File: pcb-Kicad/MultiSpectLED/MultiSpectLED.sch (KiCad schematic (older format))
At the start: 117 parts, among them J1 Conn_01x02_Female, J2 USB_C_Receptacle_USB2.0, SW1 NKK_HEXADEC, SW2 NKK_HEXADEC, U1 PAM2804, U10 PAM2804, U11 PAM2804, U12 PAM2804, U13 PAM2804, U14 PAM2804, U15 PAM2804, U16 PAM2804, U2 TeensyLC, U3 PAM2804, U4 PAM2804, U5 PAM2804, U6 PAM2804, U7 PAM2804, U8 PAM2804, U9 PAM2804

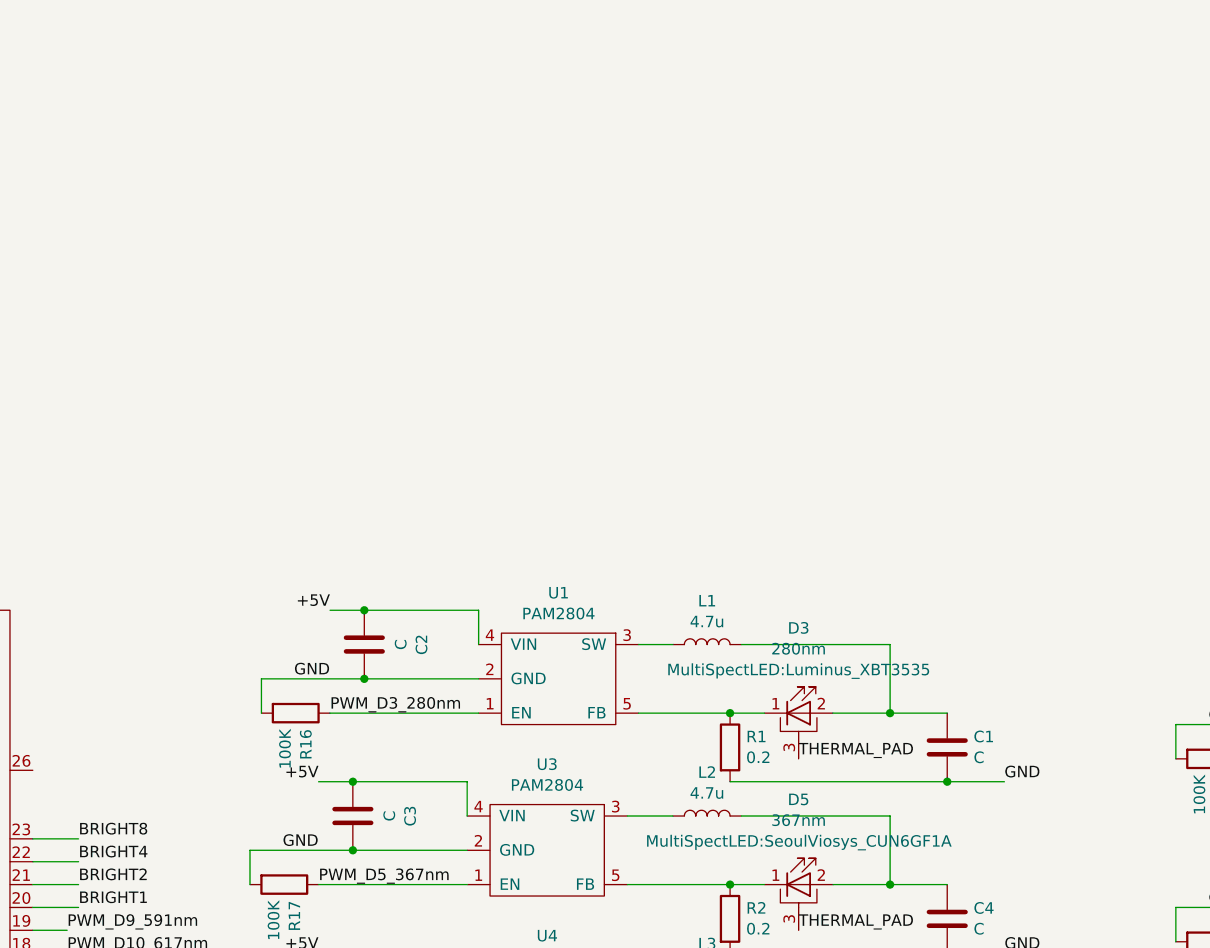
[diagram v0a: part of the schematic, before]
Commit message: Use boost driver for 280nm LED
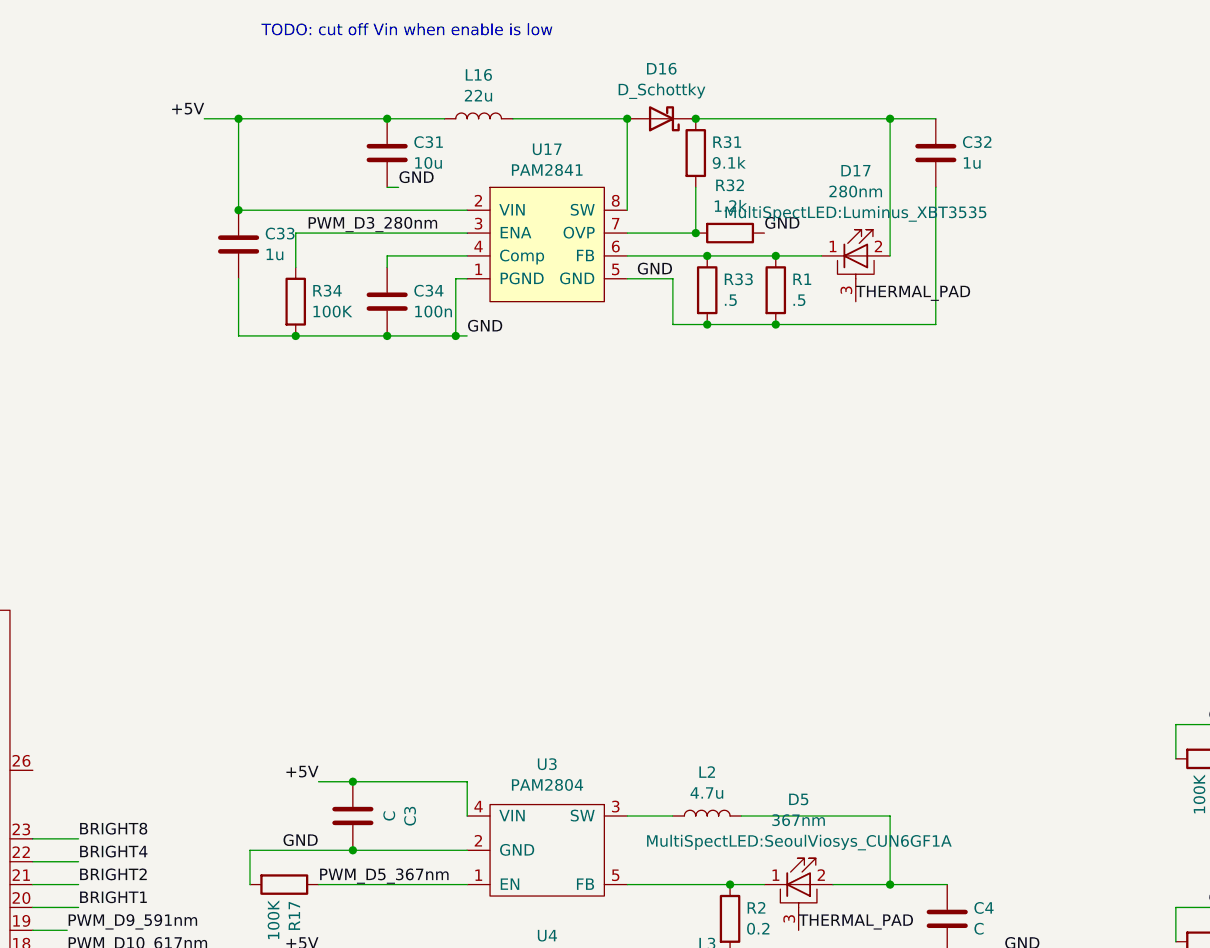
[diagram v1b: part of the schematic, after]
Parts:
- removed C1, C2: C, MultiSpectLED:C_0805_2012Metric, symbol MultiSpectLED:C
- removed D3: 280nm, MultiSpectLED:Luminus_XBT3535, symbol MultiSpectLED:LED_PAD
- removed L1: 4.7u, MultiSpectLED:L_1007_2518Metric, symbol MultiSpectLED:L
- removed R1: 0.2, MultiSpectLED:R_0805_2012Metric, symbol MultiSpectLED:R
- removed R16: 100K, MultiSpectLED:R_0402_1005Metric, symbol MultiSpectLED:R
- removed U1: PAM2804, MultiSpectLED:SOT-23-5, symbol MultiSpectLED:PAM2804
- added C31: 10u, MultiSpectLED:C_0805_2012Metric, symbol Device:C
- added C32, C33: 1u, MultiSpectLED:C_0805_2012Metric, symbol Device:C
- added C34: 100n, Capacitor_SMD:C_0402_1005Metric, symbol Device:C
- added D16: D_Schottky, Diode_SMD:D_TUMD2, symbol Device:D_Schottky
- added D17: 280nm, MultiSpectLED:Luminus_XBT3535, symbol MultiSpectLED:LED_PAD
- added L16: 22u, Inductor_SMD:L_Taiyo-Yuden_NR-50xx, symbol MultiSpectLED:L
- added R1, R33: .5, Resistor_SMD:R_0603_1608Metric, symbol Device:R
- added R31: 9.1k, MultiSpectLED:R_0402_1005Metric, symbol Device:R
- added R32: 1.2k, MultiSpectLED:R_0402_1005Metric, symbol Device:R
- added R34: 100K, MultiSpectLED:R_0402_1005Metric, symbol MultiSpectLED:R
- added U17: PAM2841, Package_SO:MSOP-8_3x3mm_P0.65mm, symbol MultiSpectLED:PAM2841
- J2: Digikey Part Number CP-036AHPJCT-ND -> 12401610E4#2ACT-ND
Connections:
- net +5V: now also C31.2, C33.1, L16.1, U17.2 (VIN)
- net GND: now also C31.1, C32.2, C33.2, C34.2, D17.3 (PAD), R1.2, R32.1, R33.2, R34.2, U17.1 (PGND), U17.5 (GND)
- net PWM_D3_280nm: now also R34.1, U17.3 (ENA)
- new net: C34.1, U17.4 (Comp)
- new net: D17.1 (K), R1.1, R33.1, U17.6 (FB)
- new net: R31.2, R32.2, U17.7 (OVP)
- new net: D16.2 (A), L16.2, U17.8 (SW)
- new net: C32.1, D16.1 (K), D17.2 (A), R31.1
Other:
- note added: "TODO: cut off Vin when enable is low"
